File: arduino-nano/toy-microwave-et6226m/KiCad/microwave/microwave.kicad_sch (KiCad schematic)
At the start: 58 parts, among them J1 Screw_Terminal_01x02, J2 Screw_Terminal_01x08, U1 ATmega328PB-A, U2 CA56-12EWA, U4 TPS563200, Y1 Crystal_Small

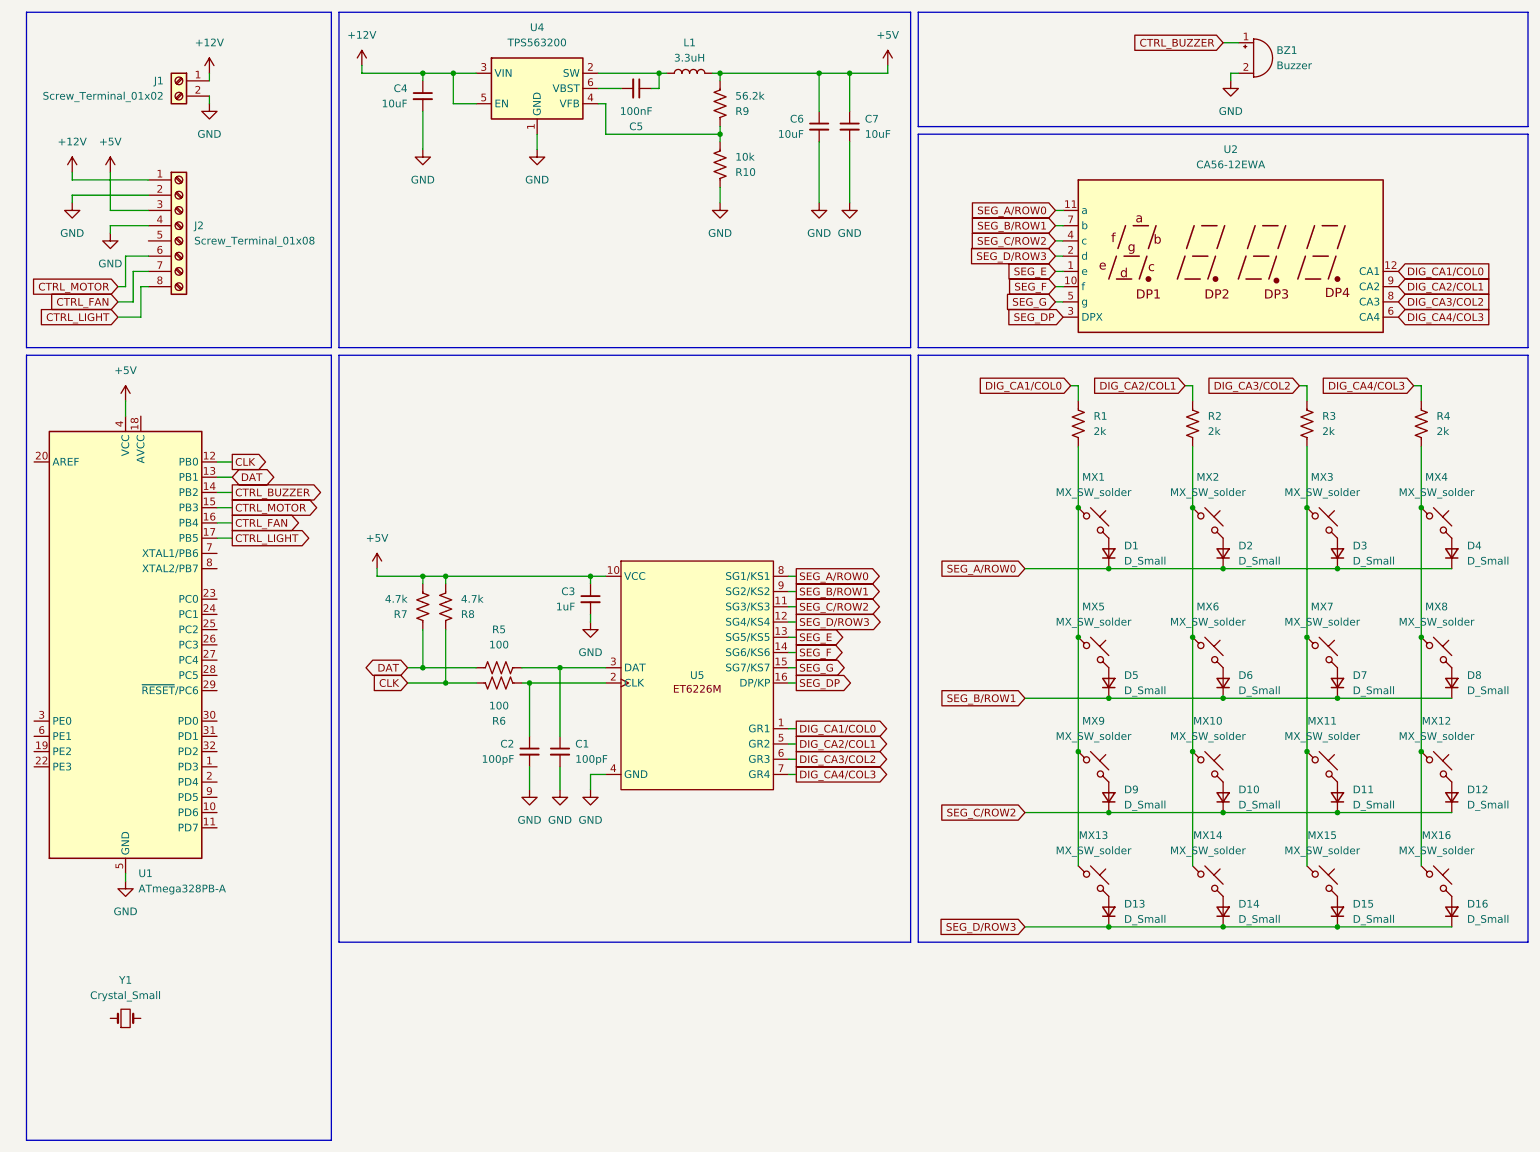
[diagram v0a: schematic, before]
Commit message: fix(toy-microwave-et6226m): mount an Arduino Nano module, add 5V rail backfeed protection
- What: replaced the bare ATmega328PB-based MCU section with an Arduino Nano v3.x module mounted directly to the board; removed the unused/fully-unwired MCP2221A USB bridge chip left over from earlier exploration; added D17 (SS14 Schottky) in series with the TPS563200 buck converter's output, and a NetTie joining the buck's diode-protected output to the Nano's 5V pin on the shared +5V net.
- Why: the board can be powered via USB (through the Nano's own onboard regulator) or via 12V (through the buck converter) at the same time, and without protection either source could backfeed into the other -- worst case, into the USB host through the Nano's own port.
- How: D17 blocks the shared rail from backfeeding into the buck converter; the Nano module's own internal VUSB-to-5V diode (confirmed against Gravitech's schematic) independently blocks the rail from backfeeding into USB, so both directions are covered without touching the Nano's 5V pin directly. The NetTie keeps the two nets named distinctly in the schematic while joining them electrically, avoiding an ERC "multiple power-output pins" false positive.
- Benefit: USB and 12V can be connected simultaneously (e.g. programming while the board is powered) with no risk to either source, and the schematic now only reflects the MCU approach actually being built.
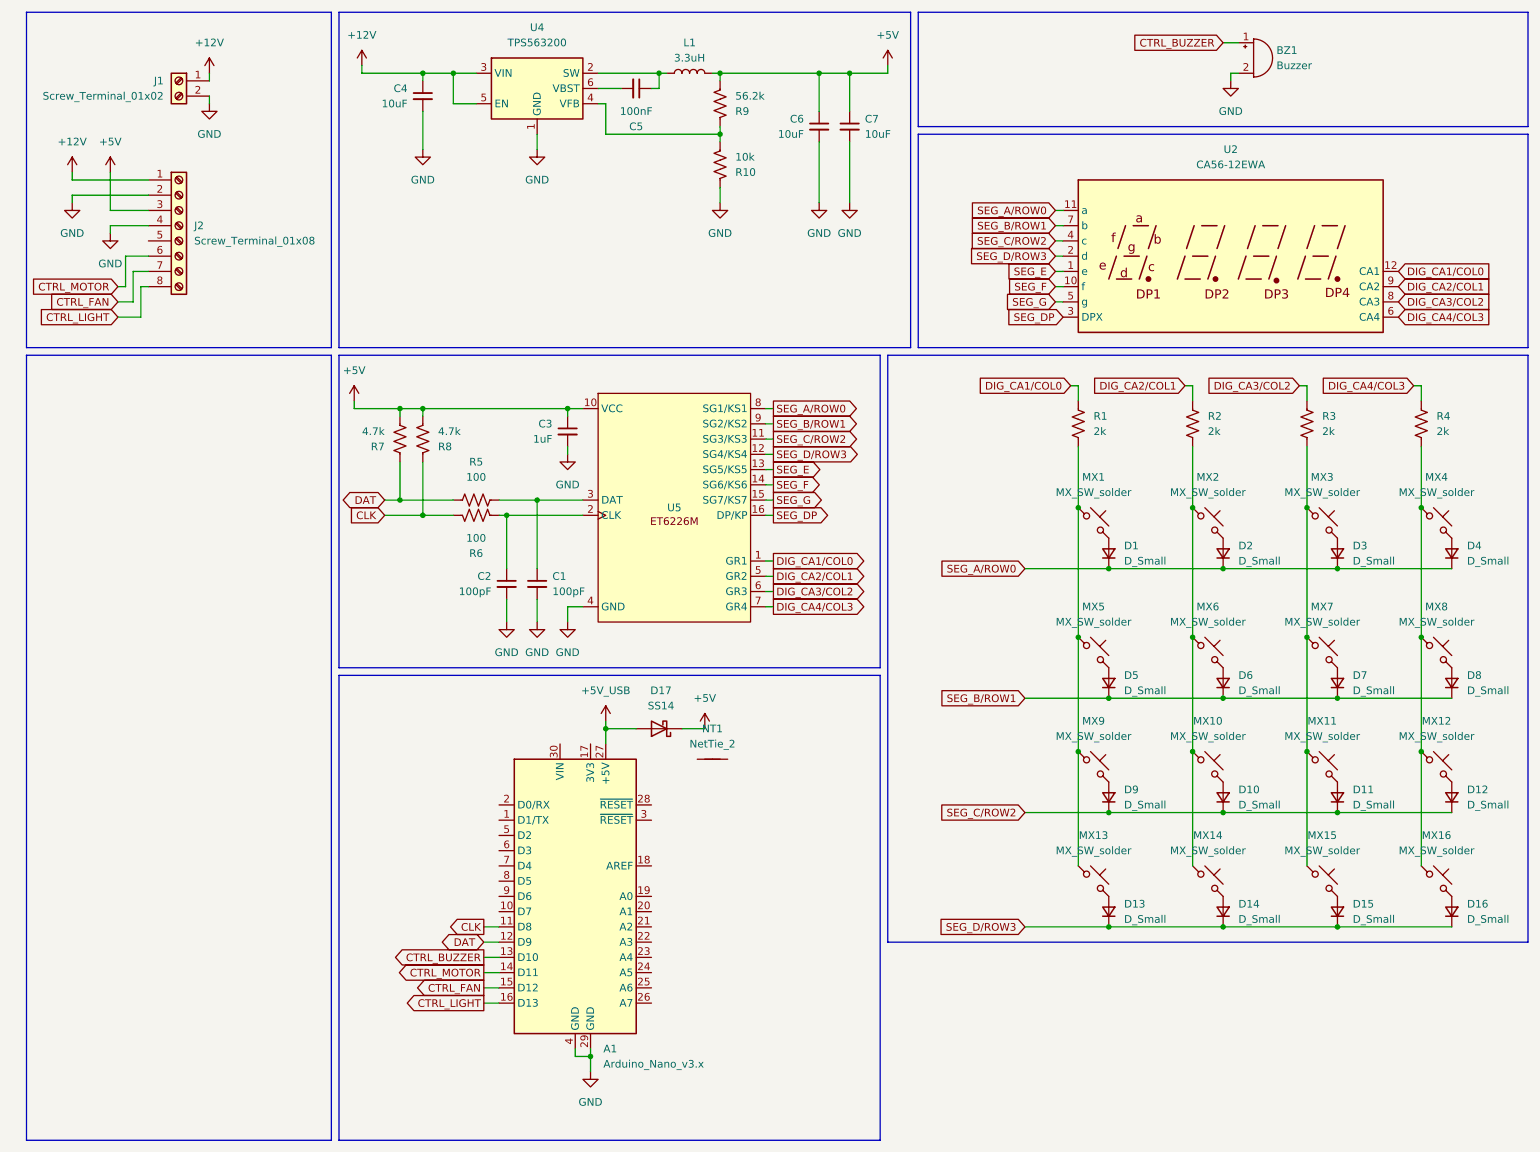
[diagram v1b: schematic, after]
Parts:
- removed U1: ATmega328PB-A, Package_QFP:TQFP-32_7x7mm_P0.8mm, symbol MCU_Microchip_ATmega:ATmega328PB-A
- removed Y1: Crystal_Small, symbol Device:Crystal_Small
- added A1: Arduino_Nano_v3.x, Module:Arduino_Nano, symbol MCU_Module:Arduino_Nano_v3.x
- added D17: SS14, Diode_SMD:D_SMA, symbol Diode:SS14
- added NT1: NetTie_2, symbol Device:NetTie_2
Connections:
- net +5V: now also D17.1 (K)
- net CLK: now also A1.11 (D8)
- net CTRL_BUZZER: now also A1.13 (D10)
- net CTRL_FAN: now also A1.15 (D12)
- net CTRL_LIGHT: now also A1.16 (D13)
- net CTRL_MOTOR: now also A1.14 (D11)
- net DAT: now also A1.12 (D9)
- net GND: now also A1.29 (GND), A1.4 (GND)
- new net +5V_USB: A1.27 (+5V), D17.2 (A)
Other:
- moved on the sheet: C1, C2, C3, R5, R6, R7, R8, U5

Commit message: feat(toy-microwave-et6226m): swap to AP63205 buck, fix 5V rail ORing, lay out PCB
- What: replaced the TPS563200 buck converter (U1) with the AP63205 (fixed 5V output, deleting the R9/R10 feedback divider), updated L1 to 4.7uH and C6/C7 to 22uF per its datasheet, added a CTRL_MISC signal on D6 alongside the existing motor/fan/light/buzzer controls, and completed the PCB layout with DRC run clean (the only remaining items are NPTH-inside-courtyard warnings between keypad diodes and adjacent MX switch mounting pegs, confirmed as no physical interference in the 3D viewer and excluded with a note).
- Why: the fixed-output AP63205 removes two passives and a divider that could be mis-valued; the 5V rail is fed from two sources (USB, through the Nano module, and 12V through the buck) that can both be connected at once, and needed protection so neither can backfeed the other.
- How: D17 (SS14 Schottky) sits between the buck's raw output and the shared +5V net -- not between the Nano's 5V pin and the rail, since that pin has to act as both a source (USB-powered) and a sink (buck-powered) and a single diode can't support both directions. The Nano's own internal diode (Gravitech's SS1P3L, between VUSB and its 5V pin) independently protects the USB/host side. A NetTie keeps the buck's raw-output net and the shared rail distinctly named in the schematic while ERC treats the join as intentional.
- Benefit: USB and 12V can be connected simultaneously in any combination without risking the buck converter, the Nano, or the USB host, and the PCB is routed and DRC-clean.
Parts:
- removed J1: Screw_Terminal_01x02, TerminalBlock_Phoenix:TerminalBlock_Phoenix_MPT-0,5-2-2.54_1x02_P2.54mm_Horizontal, symbol Connector:Screw_Terminal_01x02
- removed J2: Screw_Terminal_01x08, TerminalBlock_Phoenix:TerminalBlock_Phoenix_MKDS-1,5-8_1x08_P5.00mm_Horizontal, symbol Connector:Screw_Terminal_01x08
- removed NT1: NetTie_2, symbol Device:NetTie_2
- removed R10: 10k, Resistor_SMD:R_0805_2012Metric_Pad1.20x1.40mm_HandSolder, symbol Device:R_US
- removed R9: 56.2k, Resistor_SMD:R_0805_2012Metric_Pad1.20x1.40mm_HandSolder, symbol Device:R_US
- removed U4: TPS563200, Package_TO_SOT_SMD:SOT-23-6, symbol Regulator_Switching:TPS563200
- added H1, H2, H3, H4: MountingHole_Pad, MountingHole:MountingHole_3.2mm_M3_Pad_Via, symbol Mechanical:MountingHole_Pad
- added J1, J2: Screw_Terminal_01x04, TerminalBlock_Phoenix:TerminalBlock_Phoenix_MKDS-1,5-4-5.08_1x04_P5.08mm_Horizontal, symbol Connector:Screw_Terminal_01x04
- added U1: AP63205WU, Package_TO_SOT_SMD:TSOT-23-6, symbol Regulator_Switching:AP63205WU
- BZ1: footprint (none) -> Buzzer_Beeper:Buzzer_12x9.5RM7.6
- C4: footprint Capacitor_SMD:C_0805_2012Metric_Pad1.18x1.45mm_HandSolder -> Capacitor_SMD:C_1210_3225Metric_Pad1.33x2.70mm_HandSolder
- C6, C7: value 10uF -> 22uF; footprint Capacitor_SMD:C_0805_2012Metric_Pad1.18x1.45mm_HandSolder -> Capacitor_SMD:C_1210_3225Metric_Pad1.33x2.70mm_HandSolder
- L1: value 3.3uH -> 4.7uH; footprint (none) -> Inductor_SMD:L_Murata_LQH55DN_5.7x5.0mm
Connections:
- net +12V: now also J1.1 (Pin_1), U1.2 (EN), U1.3 (IN)
- net +5V: now also A1.27 (+5V), J1.4 (Pin_4); no longer C6.1, C7.1, L1.2
- net CTRL_FAN: now also J2.2 (Pin_2)
- net CTRL_LIGHT: now also J2.3 (Pin_3)
- net CTRL_MOTOR: now also J2.1 (Pin_1)
- net GND: now also H1.1, H2.1, H3.1, H4.1, J1.2 (Pin_2), J1.3 (Pin_3), U1.4 (GND)
- net at C5.1, L1.1: now also U1.5 (SW)
- net at C5.2: now also U1.6 (BST)
- net CTRL_MISC: now reaches A1.9 (D6)
- net CTRL_MISC: now also J2.4 (Pin_4)
- net +5V_USB renamed VOUT_5V
- net VOUT_5V: now also C6.1, C7.1, L1.2, U1.1 (FB); no longer A1.27 (+5V)
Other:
- moved on the sheet: C6, C7, D17

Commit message: fix(toy-microwave-et6226m): swap to a common-cathode display and drive the buzzer through a MOSFET
- What: U2 becomes CC56-12SURKWA, BZ1 moves low-side behind AO3400A Q2 with R9/R10 and SS14 flyback D18, D1-D16 are valued 1N4148W, U5 loads from the shared embedded library, and the BOM export is regenerated.
- Why: the ET6226M sources segments and sinks grids so a common-anode display never lights, and the 42 ohm coil drew about 119 mA from a pin rated 40 mA.
- How: pin-for-pin display swap on the same footprint, a gate-resistor and pull-down MOSFET stage clamped to +5V, and a project sym-lib-table pointing at kicad/embedded.kicad_sym.
- Benefit: the display lights, the buzzer no longer overloads D10, and ERC and DRC run clean.
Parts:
- removed U2: CA56-12EWA, Display_7Segment:CA56-12EWA, symbol Display_Character:CA56-12EWA
- added D18: SS14, Diode_SMD:D_SMA, symbol Diode:SS14
- added Q2: AO3400A, Package_TO_SOT_SMD:SOT-23, symbol Transistor_FET:AO3400A
- added R10: 4.7k, Resistor_SMD:R_0805_2012Metric_Pad1.20x1.40mm_HandSolder, symbol Device:R_US
- added R9: 100, Resistor_SMD:R_0805_2012Metric_Pad1.20x1.40mm_HandSolder, symbol Device:R_US
- added U2: CC56-12SURKWA, Display_7Segment:CA56-12SURKWA, symbol Display_Character:CC56-12SURKWA
- D1, D10, D11, D12, D13, D14, D15, D16, D2, D3, D4, D5, D6, D7, D8, D9: value D_Small -> 1N4148W
- U5: value (none) -> ET6226M; symbol Driver_Display:ET6226M -> embedded:ET6226M
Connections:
- net +5V: now also BZ1.1 (+), D18.1 (K)
- net CTRL_BUZZER: now also R9.1; no longer BZ1.1 (+)
- net DIG_CA1/COL0: now also U2.12 (CC1)
- net DIG_CA2/COL1: now also U2.9 (CC2)
- net DIG_CA3/COL2: now also U2.8 (CC3)
- net DIG_CA4/COL3: now also U2.6 (CC4)
- net GND: now also Q2.2 (S), R10.1; no longer BZ1.2 (-)
- net SEG_A/ROW0: now also U2.11 (a)
- net SEG_B/ROW1: now also U2.7 (b)
- net SEG_C/ROW2: now also U2.4 (c)
- net SEG_DP: now also U2.3 (DPX)
- net SEG_D/ROW3: now also U2.2 (d)
- net SEG_E: now also U2.1 (e)
- net SEG_F: now also U2.10 (f)
- net SEG_G: now also U2.5 (g)
- new net: BZ1.2 (-), D18.2 (A), Q2.3 (D)
- new net: Q2.1 (G), R10.2, R9.2
- no-connect marks 0 -> 20
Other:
- moved on the sheet: BZ1

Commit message: refactor(toy-microwave-et6226m): move the layout onto the mil standard
- What: sets every track to 10, 20, or 60 mil and every via to 24/12 mil, swaps H1-H4 to MountingHole_3.2mm_M3_ISO7380_Pad_TopBottom in the schematic and PCB, adds Default (10 mil) and Power (20 mil) net classes at 8 mil clearance, and adds 10/20/60 mil track and 24/12 mil via predefined sizes.
- Why: the board mixed 7.87, 9.84, 25, and 30 mil tracks with three via sizes, and the Pad_Via mounting holes sat 0.3 mm from the edge against a 0.5 mm rule.
- How: rescaled widths and vias in place, swapped each hole footprint at its existing position, and spread the 40 track pairs that sat at 0.2 mm to meet 8 mil clearance.
- Benefit: DRC reports 0 clearance, edge, and unconnected errors, and new tracks default to standard mil widths.
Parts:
- H1, H2, H3, H4: footprint MountingHole:MountingHole_3.2mm_M3_Pad_Via -> MountingHole:MountingHole_3.2mm_M3_ISO7380_Pad_TopBottom
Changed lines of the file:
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@@
 			)
 		)
-		(property "Footprint" "MountingHole:MountingHole_3.2mm_M3_Pad_Via"
+		(property "Footprint" "MountingHole:MountingHole_3.2mm_M3_ISO7380_Pad_TopBottom"
 			(at 25.4 96.52 0)
 			(hide yes)
@@
 			)
 		)
-		(property "Footprint" "MountingHole:MountingHole_3.2mm_M3_Pad_Via"
+		(property "Footprint" "MountingHole:MountingHole_3.2mm_M3_ISO7380_Pad_TopBottom"
 			(at 25.4 105.41 0)
 			(hide yes)
@@
 			)
 		)
-		(property "Footprint" "MountingHole:MountingHole_3.2mm_M3_Pad_Via"
+		(property "Footprint" "MountingHole:MountingHole_3.2mm_M3_ISO7380_Pad_TopBottom"
 			(at 25.4 78.74 0)
 			(hide yes)
@@
 			)
 		)
-		(property "Footprint" "MountingHole:MountingHole_3.2mm_M3_Pad_Via"
+		(property "Footprint" "MountingHole:MountingHole_3.2mm_M3_ISO7380_Pad_TopBottom"
 			(at 25.4 87.63 0)
 			(hide yes)
